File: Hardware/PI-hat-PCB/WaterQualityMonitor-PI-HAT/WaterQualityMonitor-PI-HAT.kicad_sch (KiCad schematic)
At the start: 0 parts

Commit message: Added LED schematic
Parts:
- added C?: 10uF, symbol Device:C
- added C?: 2uF, symbol Device:C
- added D?: OVLEW1CB9, LED_5MM, symbol SparkFun-LED:LED5MM
- added L?: 22uH, symbol pspice:INDUCTOR
- added R?: 10, symbol Device:R
- added U?: TPS61158DRVR, SON65P200X200X80-7N, symbol TPS61158DRVR:TPS61158DRVR
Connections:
- new net: C?.1, D?.A, U?.3 (VOUT)
- new net: D?.K (C), R?.1, U?.4 (FB)
- new net: L?.2, U?.6 (LX)
- new net +5V: C?.1, L?.1, U?.2 (VIN)
- new net CTRLLED: U?.1 (CTRL)
- new net GND: C?.2, C?.2, U?.5 (GND)
- new net GNDA: R?.2, U?.7 (THERMALPAD)
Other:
- note added: "Microscope LED"

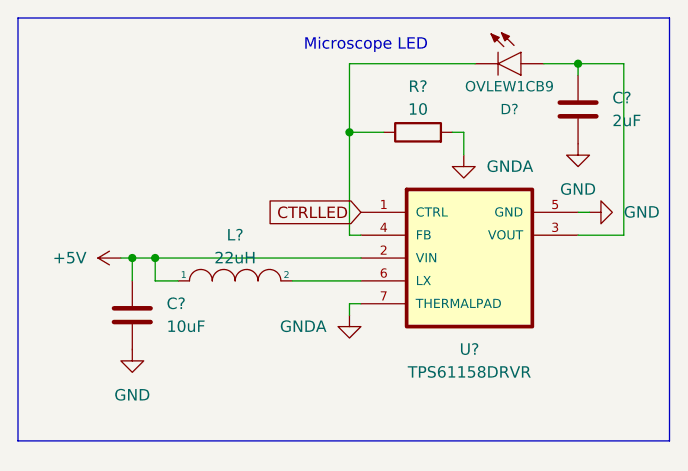
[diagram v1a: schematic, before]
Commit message: Updated and corrected LED schematic
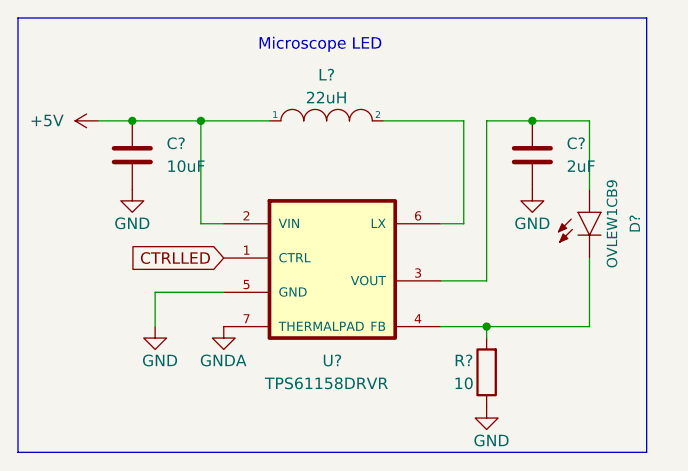
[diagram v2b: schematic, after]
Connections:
- net GND: now also R?.1
- net GNDA: no longer R?.2
- net at D?.K (C), U?.4 (FB): now also R?.2; no longer R?.1
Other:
- moved on the sheet: C?, D?, L?, R?, U?

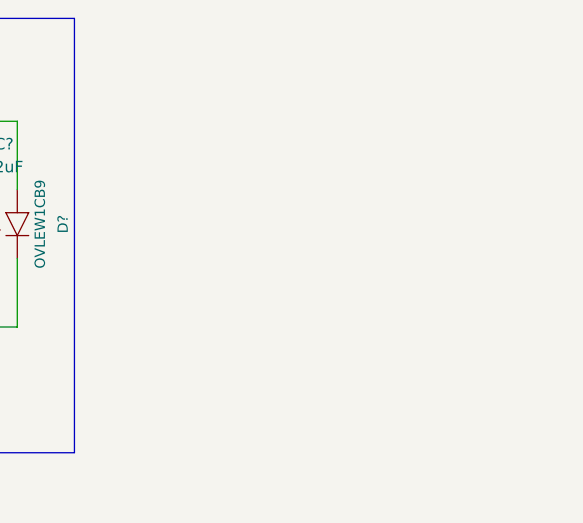
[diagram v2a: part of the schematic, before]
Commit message: Started Stepper motor controller
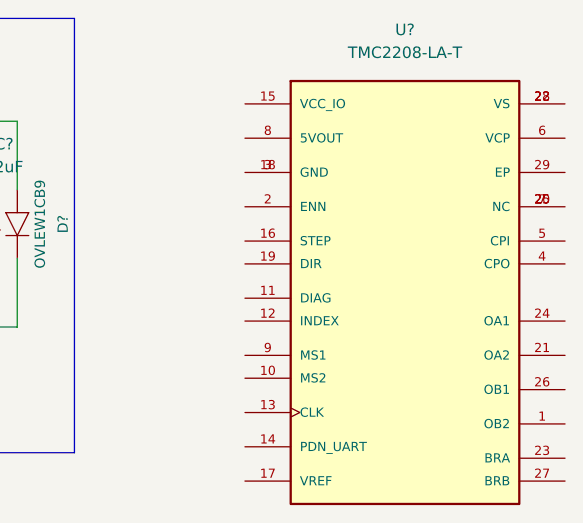
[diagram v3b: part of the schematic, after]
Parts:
- added U?: TMC2208-LA-T, QFN50P500X500X90-29N, symbol TMC2208-LA-T:TMC2208-LA-T
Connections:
- new net: U?.18 (GND), U?.3 (GND)
- new net: U?.20 (NC), U?.25 (NC), U?.7 (NC)
- new net: U?.22 (VS), U?.28 (VS)
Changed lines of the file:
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@@
     )
   )
-  (symbol (lib_id "power:GND") (at 27.94 46.99 0) (unit 1)
-    (in_bom yes) (on_board yes) (fields_autoplaced)
-    (property "Reference" "#PWR?" (id 0) (at 27.94 53.34 0)
-      (effects (font (size 1.27 1.27)) hide)
-    )
-    (property "Value" "GND" (id 1) (at 30.48 50.8 0)
-      (effects (font (size 1.27 1.27)) (justify right))
-    )
-    (property "Footprint" "" (id 2) (at 27.94 46.99 0)
-      (effects (font (size 1.27 1.27)) hide)
-    )
-    (property "Datasheet" "" (id 3) (at 27.94 46.99 0)
-      (effects (font (size 1.27 1.27)) hide)
-    )
-    (pin "1")
-  )
-  (symbol (lib_id "power:GND") (at 25.4 31.75 0) (unit 1)
-    (in_bom yes) (on_board yes)
-    (property "Reference" "#PWR?" (id 0) (at 25.4 38.1 0)
-      (effects (font (size 1.27 1.27)) hide)
-    )
-    (property "Value" "GND" (id 1) (at 25.4 35.56 0))
-    (property "Footprint" "" (id 2) (at 25.4 31.75 0)
-      (effects (font (size 1.27 1.27)) hide)
-    )
-    (property "Datasheet" "" (id 3) (at 25.4 31.75 0)
-      (effects (font (size 1.27 1.27)) hide)
-    )
-    (pin "1")
-  )
-  (symbol (lib_id "power:GND") (at 69.85 31.75 0) (unit 1)
-    (in_bom yes) (on_board yes)
-    (property "Reference" "#PWR?" (id 0) (at 69.85 38.1 0)
-      (effects (font (size 1.27 1.27)) hide)
-    )
-    (property "Value" "GND" (id 1) (at 69.85 35.56 0))
-    (property "Footprint" "" (id 2) (at 69.85 31.75 0)
-      (effects (font (size 1.27 1.27)) hide)
-    )
-    (property "Datasheet" "" (id 3) (at 69.85 31.75 0)
-      (effects (font (size 1.27 1.27)) hide)
-    )
-    (pin "1")
-  )
-  (symbol (lib_id "TPS61158DRVR:TPS61158DRVR") (at 53.34 43.18 0) (unit 1)
-    (in_bom yes) (on_board yes) (fields_autoplaced)
-    (property "Reference" "U?" (id 0) (at 47.625 50.8 0))
-    (property "Value" "TPS61158DRVR" (id 1) (at 46.99 53.34 0))
-    (property "Footprint" "SON65P200X200X80-7N" (id 2) (at 39.37 43.18 0)
-      (effects (font (size 1.27 1.27)) (justify left bottom) hide)
-    )
-    (property "Datasheet" "" (id 3) (at 53.34 43.18 0)
-      (effects (font (size 1.27 1.27)) (justify left bottom) hide)
-    )
-    (pin "1")
-    (pin "2")
+  (symbol (lib_id "TMC2208-LA-T:TMC2208-LA-T") (at 119.2784 47.5996 0) (unit 1)
+    (in_bom yes) (on_board yes) (fields_autoplaced)
+    (property "Reference" "U?" (id 0) (at 119.2784 13.97 0))
+    (property "Value" "TMC2208-LA-T" (id 1) (at 119.2784 16.51 0))
+    (property "Footprint" "QFN50P500X500X90-29N" (id 2) (at 106.5784 42.5196 0)
+      (effects (font (size 1.27 1.27)) (justify left bottom) hide)
+    )
+    (property "Datasheet" "" (id 3) (at 119.2784 47.5996 0)
+      (effects (font (size 1.27 1.27)) (justify left bottom) hide)
+    )
+    (property "PARTREV" "1.09" (id 4) (at 112.9284 47.5996 0)
+      (effects (font (size 1.27 1.27)) (justify left bottom) hide)
+    )
+    (property "MANUFACTURER" "Trinamic Motion" (id 5) (at 111.6584 53.9496 0)
+      (effects (font (size 1.27 1.27)) (justify left bottom) hide)
+    )
+    (property "MAXIMUM_PACKAGE_HEIGHT" "0.9mm" (id 6) (at 116.7384 51.4096 0)
+      (effects (font (size 1.27 1.27)) (justify left bottom) hide)
+    )
+    (property "STANDARD" "IPC 7351B" (id 7) (at 118.0084 47.5996 0)
+      (effects (font (size 1.27 1.27)) (justify left bottom) hide)
+    )
+    (pin "1")
+    (pin "10")
+    (pin "11")
+    (pin "12")
+    (pin "13")
+    (pin "14")
+    (pin "15")
+    (pin "16")
+    (pin "17")
+    (pin "18")
+    (pin "19")
+    (pin "2")
+    (pin "20")
+    (pin "21")
+    (pin "22")
+    (pin "23")
+    (pin "24")
+    (pin "25")
+    (pin "26")
+    (pin "27")
+    (pin "28")
+    (pin "29")
     (pin "3")
     (pin "4")
@@
     (pin "6")
     (pin "7")
+    (pin "8")
+    (pin "9")
+  )
+  (symbol (lib_id "power:GND") (at 27.94 46.99 0) (unit 1)
+    (in_bom yes) (on_board yes) (fields_autoplaced)
+    (property "Reference" "#PWR?" (id 0) (at 27.94 53.34 0)
+      (effects (font (size 1.27 1.27)) hide)
+    )
+    (property "Value" "GND" (id 1) (at 30.48 50.8 0)
+      (effects (font (size 1.27 1.27)) (justify right))
+    )
+    (property "Footprint" "" (id 2) (at 27.94 46.99 0)
+      (effects (font (size 1.27 1.27)) hide)
+    )
+    (property "Datasheet" "" (id 3) (at 27.94 46.99 0)
+      (effects (font (size 1.27 1.27)) hide)
+    )
+    (pin "1")
+  )
+  (symbol (lib_id "power:GND") (at 25.4 31.75 0) (unit 1)
+    (in_bom yes) (on_board yes)
+    (property "Reference" "#PWR?" (id 0) (at 25.4 38.1 0)
+      (effects (font (size 1.27 1.27)) hide)
+    )
+    (property "Value" "GND" (id 1) (at 25.4 35.56 0))
+    (property "Footprint" "" (id 2) (at 25.4 31.75 0)
+      (effects (font (size 1.27 1.27)) hide)
+    )
+    (property "Datasheet" "" (id 3) (at 25.4 31.75 0)
+      (effects (font (size 1.27 1.27)) hide)
+    )
+    (pin "1")
+  )
+  (symbol (lib_id "power:GND") (at 69.85 31.75 0) (unit 1)
+    (in_bom yes) (on_board yes)
+    (property "Reference" "#PWR?" (id 0) (at 69.85 38.1 0)
+      (effects (font (size 1.27 1.27)) hide)
+    )
+    (property "Value" "GND" (id 1) (at 69.85 35.56 0))
+    (property "Footprint" "" (id 2) (at 69.85 31.75 0)
+      (effects (font (size 1.27 1.27)) hide)
+    )
+    (property "Datasheet" "" (id 3) (at 69.85 31.75 0)
+      (effects (font (size 1.27 1.27)) hide)
+    )
+    (pin "1")
+  )
+  (symbol (lib_id "TPS61158DRVR:TPS61158DRVR") (at 53.34 43.18 0) (unit 1)
+    (in_bom yes) (on_board yes) (fields_autoplaced)
+    (property "Reference" "U?" (id 0) (at 47.625 50.8 0))
+    (property "Value" "TPS61158DRVR" (id 1) (at 46.99 53.34 0))
+    (property "Footprint" "SON65P200X200X80-7N" (id 2) (at 39.37 43.18 0)
+      (effects (font (size 1.27 1.27)) (justify left bottom) hide)
+    )
+    (property "Datasheet" "" (id 3) (at 53.34 43.18 0)
+      (effects (font (size 1.27 1.27)) (justify left bottom) hide)
+    )
+    (pin "1")
+    (pin "2")
+    (pin "3")
+    (pin "4")
+    (pin "5")
+    (pin "6")
+    (pin "7")
   )
   (symbol (lib_id "Device:R") (at 64.77 52.07 180) (unit 1)
@@
       (reference "R?") (unit 1) (value "10") (footprint "")
     )
+    (path "/2128f533-0dfa-4d4f-8a6b-c0b85d527f97"
+      (reference "U?") (unit 1) (value "TMC2208-LA-T") (footprint "QFN50P500X500X90-29N")
+    )
     (path "/54f8c9e3-c4c0-420e-b91a-00c3873383db"

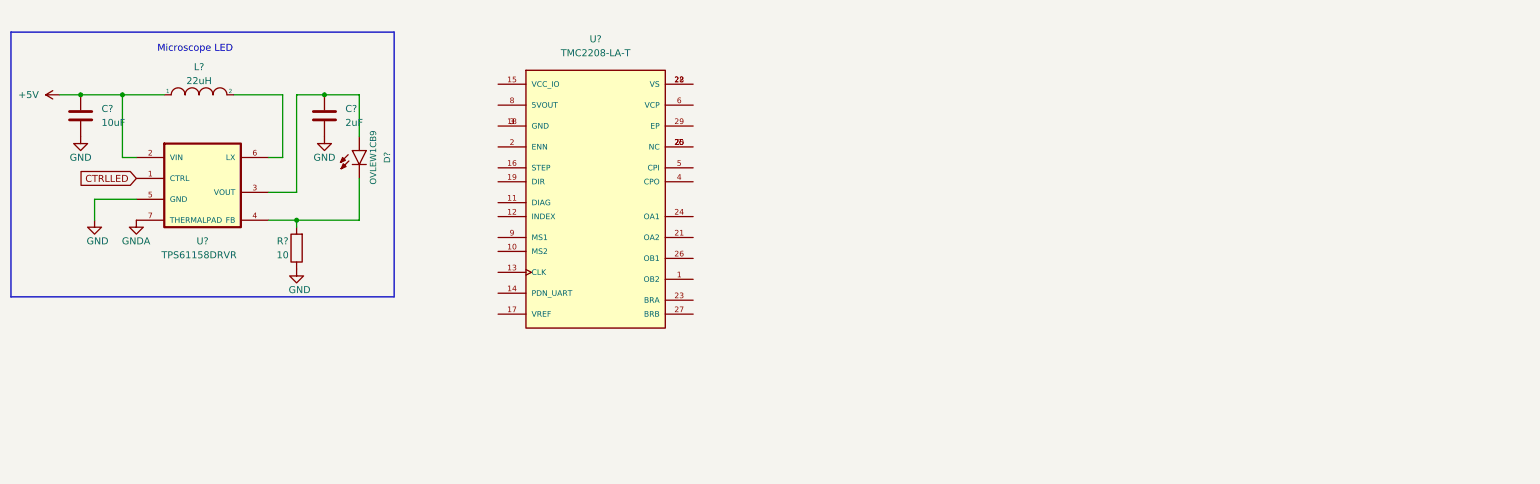
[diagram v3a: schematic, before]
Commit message: added components for stepper motor driver
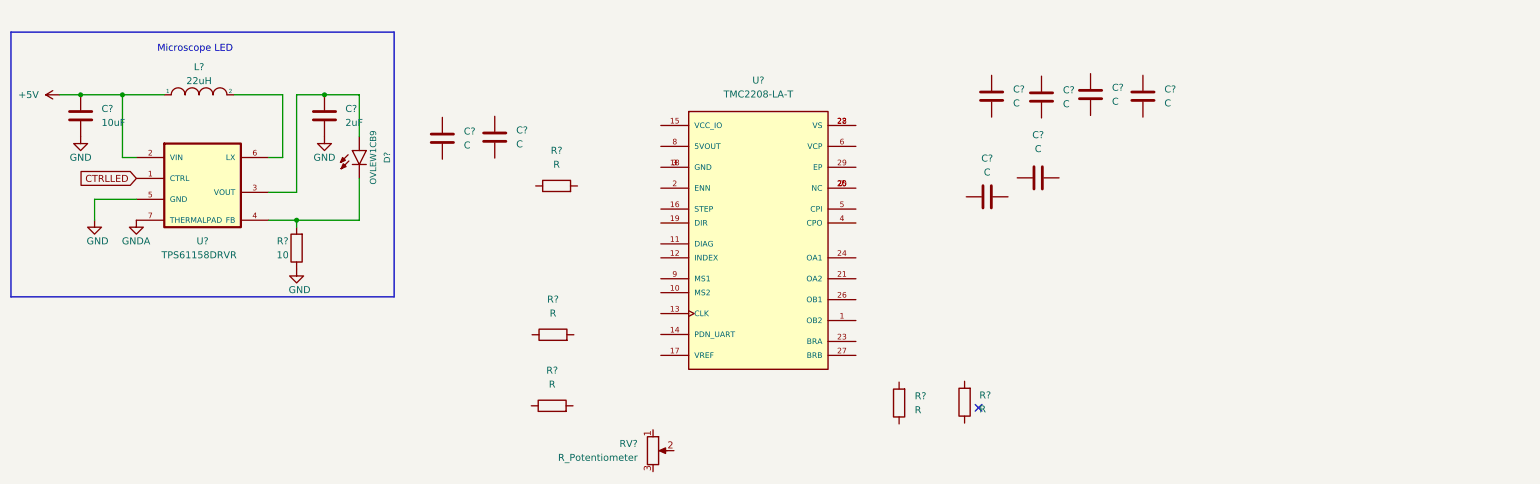
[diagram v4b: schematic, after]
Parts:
- added C? (x8): C, symbol Device:C
- added R? (x5): R, symbol Device:R
- added RV?: R_Potentiometer, symbol Device:R_Potentiometer
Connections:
- no-connect marks 0 -> 1
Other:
- moved on the sheet: U?

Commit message: worked on stepper motor driver
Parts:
- removed R?: R, symbol Device:R
- added J?: Conn_01x02_Male, symbol Connector:Conn_01x02_Male
- added JP?: SolderJumper_3_Open, symbol Jumper:SolderJumper_3_Open
- added R?: 20k, symbol Device:R
- C? (x2): value C -> 1u/50V
- C? (x4): value C -> 100n/50V
- C?: value C -> 4u7/6V3
- C?: value C -> 22n/50V
- R? (x2): value R -> 20k
- RV?: value R_Potentiometer -> 20k
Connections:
- net +5V: now also C?.2, R?.1, U?.8 (5VOUT)
- net GND: now also C?.1, C?.1, C?.1, C?.1, C?.1, C?.1, R?.1, R?.1, RV?.3, U?.13 (CLK), U?.18 (GND), U?.3 (GND), R?.2
- net at RV?.1: now also R?.2
- net VREF: now reaches RV?.2
- net VREF: now also U?.17 (VREF)
- net OB2: now reaches U?.1 (OB2)
- net MS2: now reaches U?.10 (MS2)
- net DIAG: now reaches U?.11 (DIAG)
- net INDEX: now reaches U?.12 (INDEX)
- net PDN_UART: now reaches U?.14 (PDN_UART)
- net PDN_UART: now also JP?.2 (C), R?.1
- net VIO: now reaches U?.15 (VCC_IO)
- net VIO: now also C?.2, R?.1
- net STEP: now reaches U?.16 (STEP)
- net DIR: now reaches U?.19 (DIR)
- net at U?.2 (ENN): now also R?.2
- net OA2: now reaches U?.21 (OA2)
- net VM: now reaches U?.22 (VS), U?.28 (VS)
- net VM: now also C?.2, C?.2, C?.2, C?.2, C?.2
- net at U?.23 (BRA): now also R?.2
- net OA1: now reaches U?.24 (OA1)
- net OB1: now reaches U?.26 (OB1)
- net at U?.27 (BRB): now also R?.2
- net at U?.4 (CPO): now also C?.1
- net at U?.5 (CPI): now also C?.2
- net at U?.6 (VCP): now also C?.1
- net MS1: now reaches U?.9 (MS1)
- new net: J?.2 (Pin_2), JP?.1 (A)
- new net: J?.1 (Pin_1), JP?.3 (B)
- no-connect marks 1 -> 2
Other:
- note added: "values tbd"
- moved on the sheet: C?, R?, RV?, U?

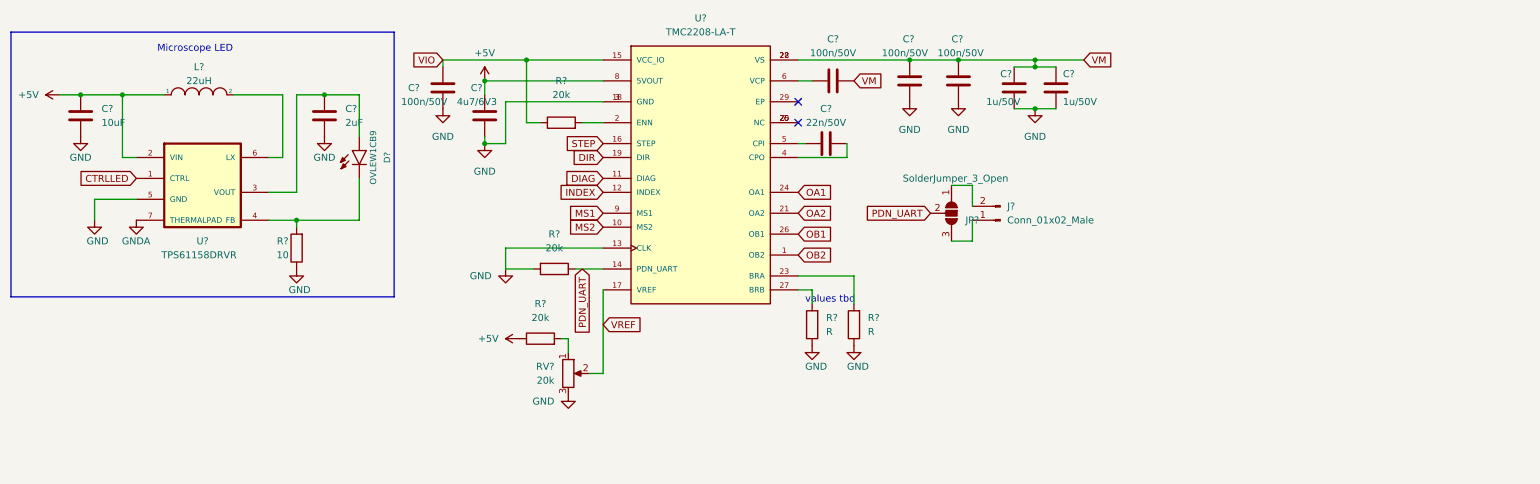
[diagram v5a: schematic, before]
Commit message: changed led IC and schematic
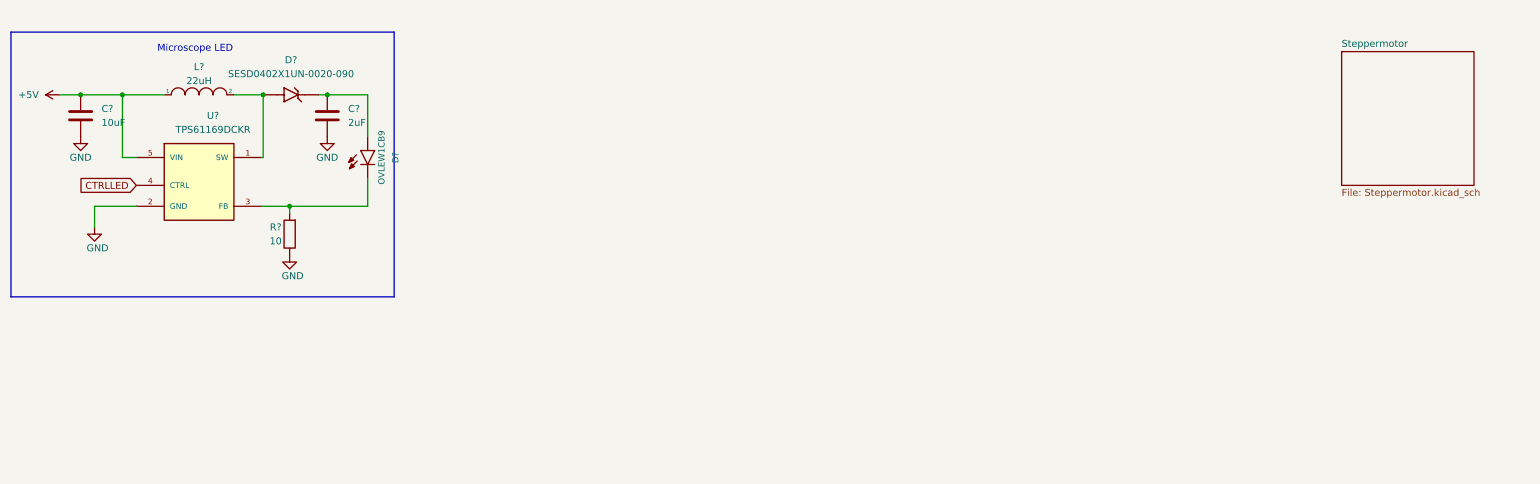
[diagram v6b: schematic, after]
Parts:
- removed C? (x2): 1u/50V, symbol Device:C
- removed C? (x4): 100n/50V, symbol Device:C
- removed C?: 4u7/6V3, symbol Device:C
- removed C?: 22n/50V, symbol Device:C
- removed J?: Conn_01x02_Male, symbol Connector:Conn_01x02_Male
- removed JP?: SolderJumper_3_Open, symbol Jumper:SolderJumper_3_Open
- removed R? (x2): R, symbol Device:R
- removed R? (x3): 20k, symbol Device:R
- removed RV?: 20k, symbol Device:R_Potentiometer
- removed U?: TMC2208-LA-T, QFN50P500X500X90-29N, symbol TMC2208-LA-T:TMC2208-LA-T
- removed U?: TPS61158DRVR, SON65P200X200X80-7N, symbol TPS61158DRVR:TPS61158DRVR
- added D?: SESD0402X1UN-0020-090, DIODFN100X60X43-2N, symbol SESD0402X1UN-0020-090:SESD0402X1UN-0020-090
- added U?: TPS61169DCKR, SOT65P210X110-5N, symbol TPS61169DCKR:TPS61169DCKR
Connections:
- net +5V: now also U?.5 (VIN)
- net CTRLLED: now also U?.4 (CTRL)
- net GND: now also U?.2 (GND)
- net at C?.1, D?.A: now also D?.C
- net at D?.K (C), R?.2: now also U?.3 (FB)
- net at L?.2: now also D?.A, U?.1 (SW)
- no-connect marks 2 -> 0
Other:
- added sheet Steppermotor (Steppermotor.kicad_sch)
- note removed: "values tbd"
- moved on the sheet: C?, D?, R?

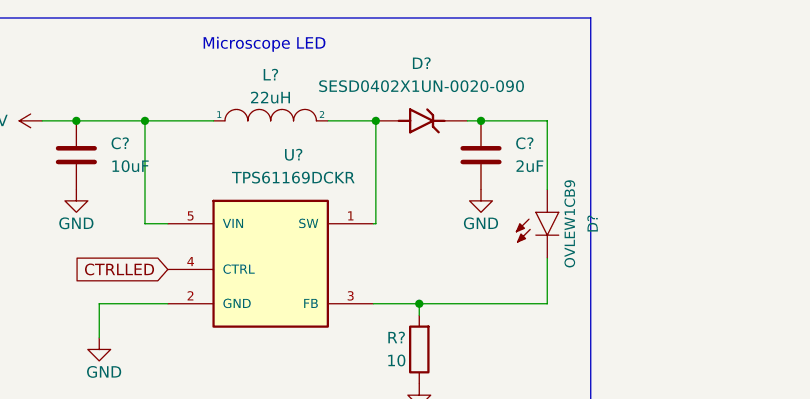
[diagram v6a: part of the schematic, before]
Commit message: changed component values
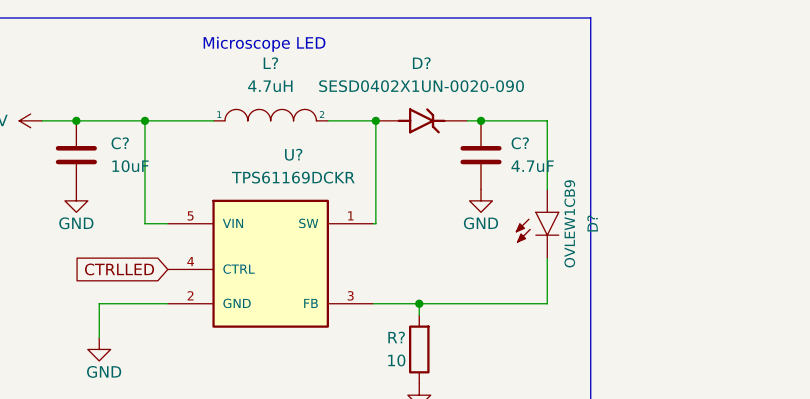
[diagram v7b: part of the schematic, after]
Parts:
- C?: value 2uF -> 4.7uF
- L?: value 22uH -> 4.7uH
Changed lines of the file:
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@@
   (symbol (lib_id "Device:C") (at 70.358 27.94 0) (unit 1)
     (in_bom yes) (on_board yes) (fields_autoplaced)
-    (property "Reference" "C?" (id 0) (at 74.168 26.6699 0)
+    (property "Reference" "C?" (id 0) (at 73.66 26.6699 0)
       (effects (font (size 1.27 1.27)) (justify left))
     )
-    (property "Value" "2uF" (id 1) (at 74.168 29.2099 0)
+    (property "Value" "4.7uF" (id 1) (at 73.66 29.2099 0)
       (effects (font (size 1.27 1.27)) (justify left))
     )
@@
   (symbol (lib_id "pspice:INDUCTOR") (at 46.99 24.13 0) (unit 1)
     (in_bom yes) (on_board yes) (fields_autoplaced)
-    (property "Reference" "L?" (id 0) (at 46.99 19.05 0))
-    (property "Value" "22uH" (id 1) (at 46.99 21.59 0))
+    (property "Reference" "L?" (id 0) (at 46.99 17.78 0))
+    (property "Value" "4.7uH" (id 1) (at 46.99 20.32 0))
     (property "Footprint" "" (id 2) (at 46.99 24.13 0)
       (effects (font (size 1.27 1.27)) hide)
@@
     )
     (path "/a35cab55-b5c2-4513-8be8-9e39b495da06"
-      (reference "C?") (unit 1) (value "2uF") (footprint "")
+      (reference "C?") (unit 1) (value "4.7uF") (footprint "")
     )
     (path "/42f59bf4-af48-4db1-8bdf-07de8825d459/aa909402-e10e-43db-9093-f526c7cd47b5"
@@
     )
     (path "/bb8ea0c7-769c-4d91-a944-5e66cb94087c"
-      (reference "L?") (unit 1) (value "22uH") (footprint "")
+      (reference "L?") (unit 1) (value "4.7uH") (footprint "")
     )
     (path "/42f59bf4-af48-4db1-8bdf-07de8825d459/466d2a04-9e85-4560-902e-ec78fc9ea78e"
